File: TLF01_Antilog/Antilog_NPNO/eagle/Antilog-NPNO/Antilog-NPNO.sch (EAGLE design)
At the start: 30 parts, among them CN1 PWRIN, IC1 NJM4580, T1 2SC1815, T2 2SC1815

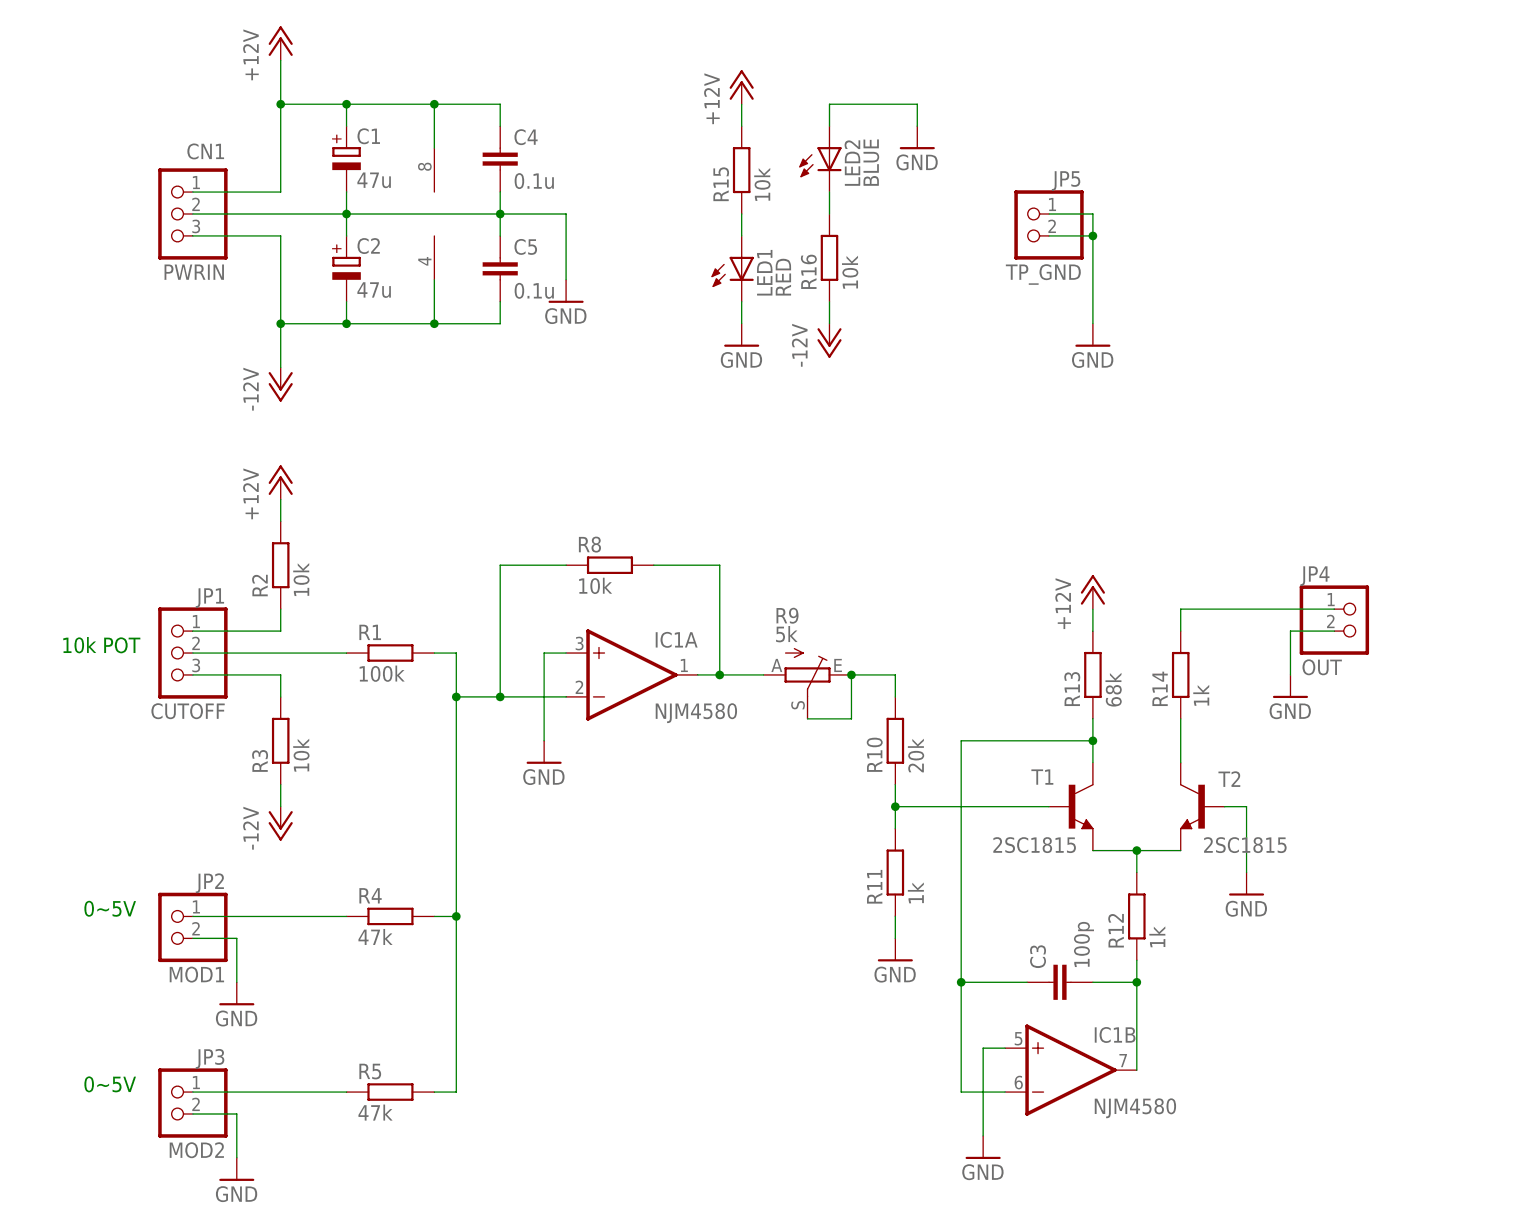
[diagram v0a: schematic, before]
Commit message: Add: Antilog_NPNO board design
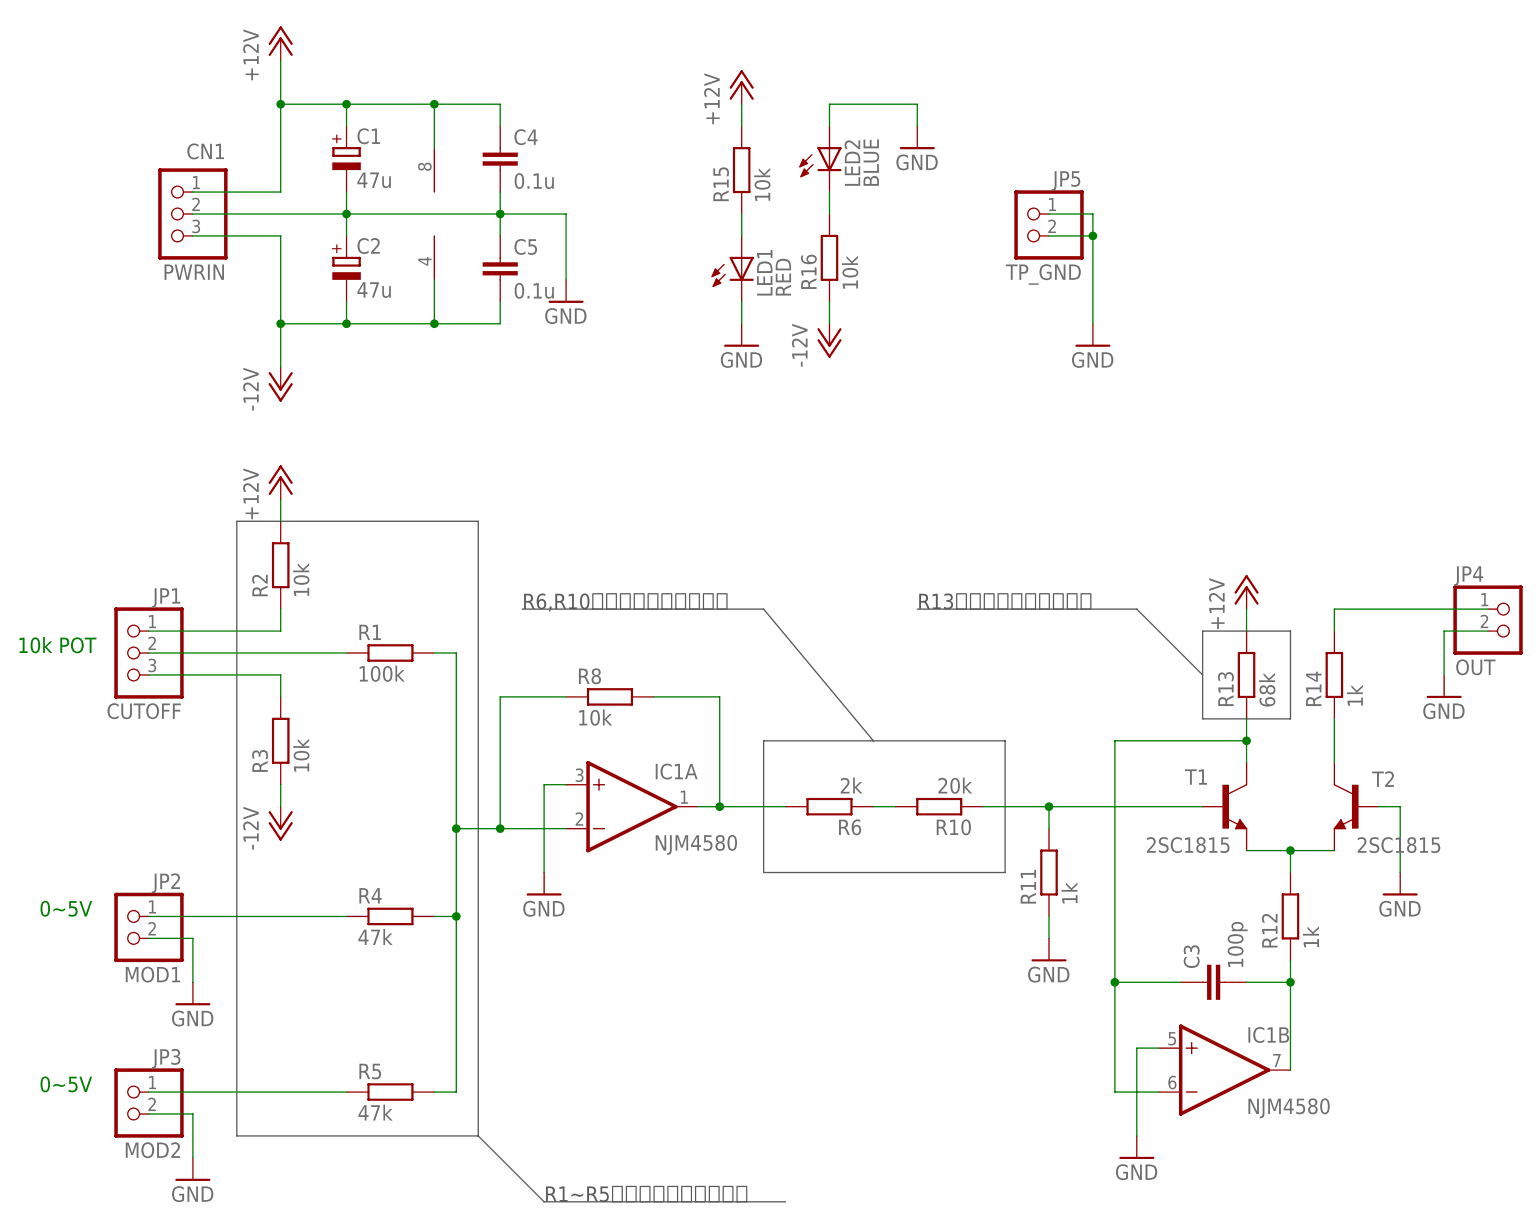
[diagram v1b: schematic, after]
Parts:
- removed R9: 5k, pot:TRIM_EU-B25P
- added R6: 2k, rcl:R-EU_0207/7
- C1, C2: device rcl:CPOL-EUE5-8.5 -> rcl:CPOL-EUE2.5-6
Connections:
- removed net N$12: R10.2, R9.E, R9.S
- new net N$6: R10.2, R6.1
- net N$5: now also R6.2; no longer R9.A
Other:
- note added: "R13はピンソケットで実装"
- note added: "R1~R5はピンソケットで実装"
- note added: "R6,R10はピンソケットで実装"
- moved on the sheet: C3, IC1A, IC1B, JP1, JP2, JP3, JP4, R10, R11, R12, R13, R14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

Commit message: Add:テスト表
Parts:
- added JP6: TP_+12V, pinhead:PINHD-1X1
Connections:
- net +12V: now also JP6.1
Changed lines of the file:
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@@
 <part name="R3" library="rcl" library_urn="urn:adsk.eagle:library:334" deviceset="R-EU_" device="0207/7" package3d_urn="urn:adsk.eagle:package:23493/1" value="10k"/>
 <part name="R6" library="rcl" library_urn="urn:adsk.eagle:library:334" deviceset="R-EU_" device="0207/7" package3d_urn="urn:adsk.eagle:package:23493/1" value="2k"/>
+<part name="JP6" library="pinhead" library_urn="urn:adsk.eagle:library:325" deviceset="PINHD-1X1" device="" package3d_urn="urn:adsk.eagle:package:22485/2" value="TP_+12V"/>
+<part name="P+3" library="supply1" library_urn="urn:adsk.eagle:library:371" deviceset="+12V" device=""/>
 </parts>
 <sheets>
@@
 <instance part="R3" gate="G$1" x="71.12" y="81.28" rot="R90"/>
 <instance part="R6" gate="G$1" x="134.62" y="73.66" rot="R180"/>
+<instance part="JP6" gate="G$1" x="177.8" y="142.24" rot="MR0"/>
+<instance part="P+3" gate="1" x="185.42" y="154.94"/>
 </instances>
 <busses>
@@
 <wire x1="71.12" y1="109.22" x2="71.12" y2="106.68" width="0.1524" layer="91"/>
 </segment>
+<segment>
+<pinref part="P+3" gate="1" pin="+12V"/>
+<wire x1="185.42" y1="152.4" x2="185.42" y2="142.24" width="0.1524" layer="91"/>
+<pinref part="JP6" gate="G$1" pin="1"/>
+<wire x1="185.42" y1="142.24" x2="180.34" y2="142.24" width="0.1524" layer="91"/>
+</segment>
 </net>
